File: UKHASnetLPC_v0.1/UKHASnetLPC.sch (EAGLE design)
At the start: 9 parts

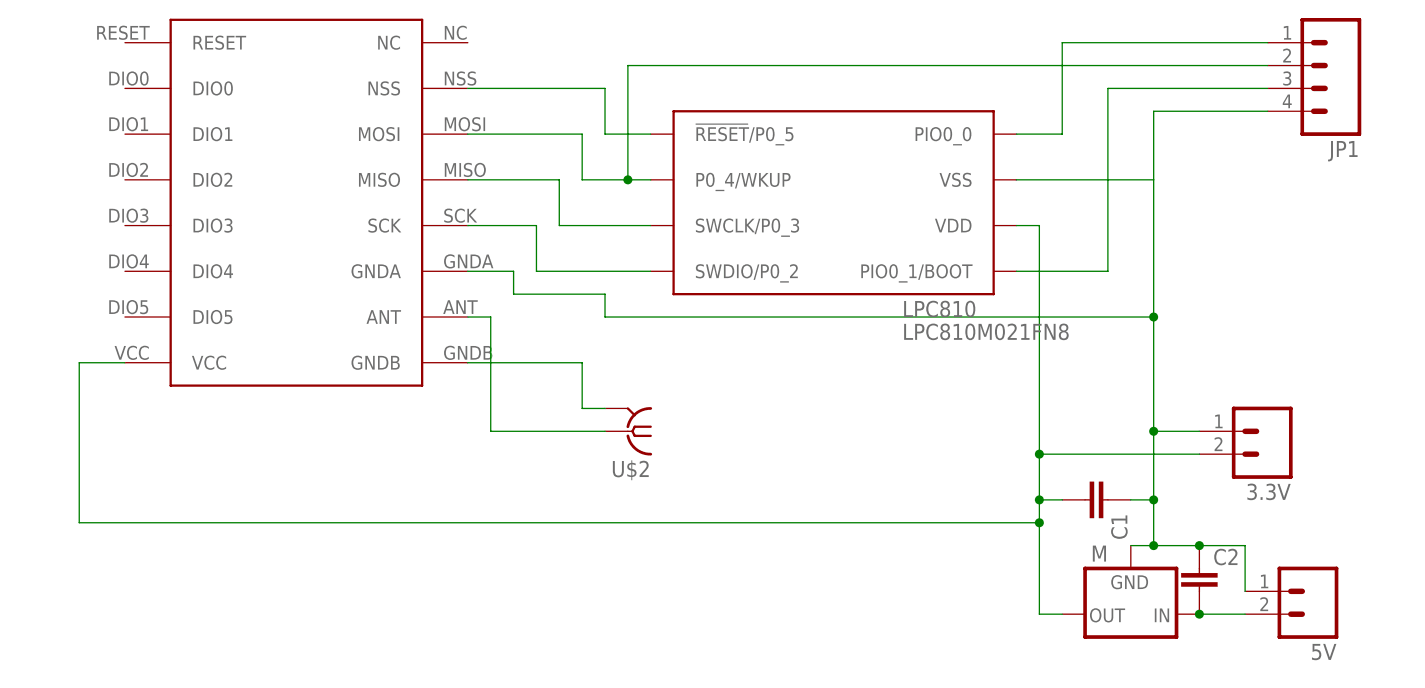
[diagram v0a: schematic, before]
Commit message: Redesigned board to avoid interference
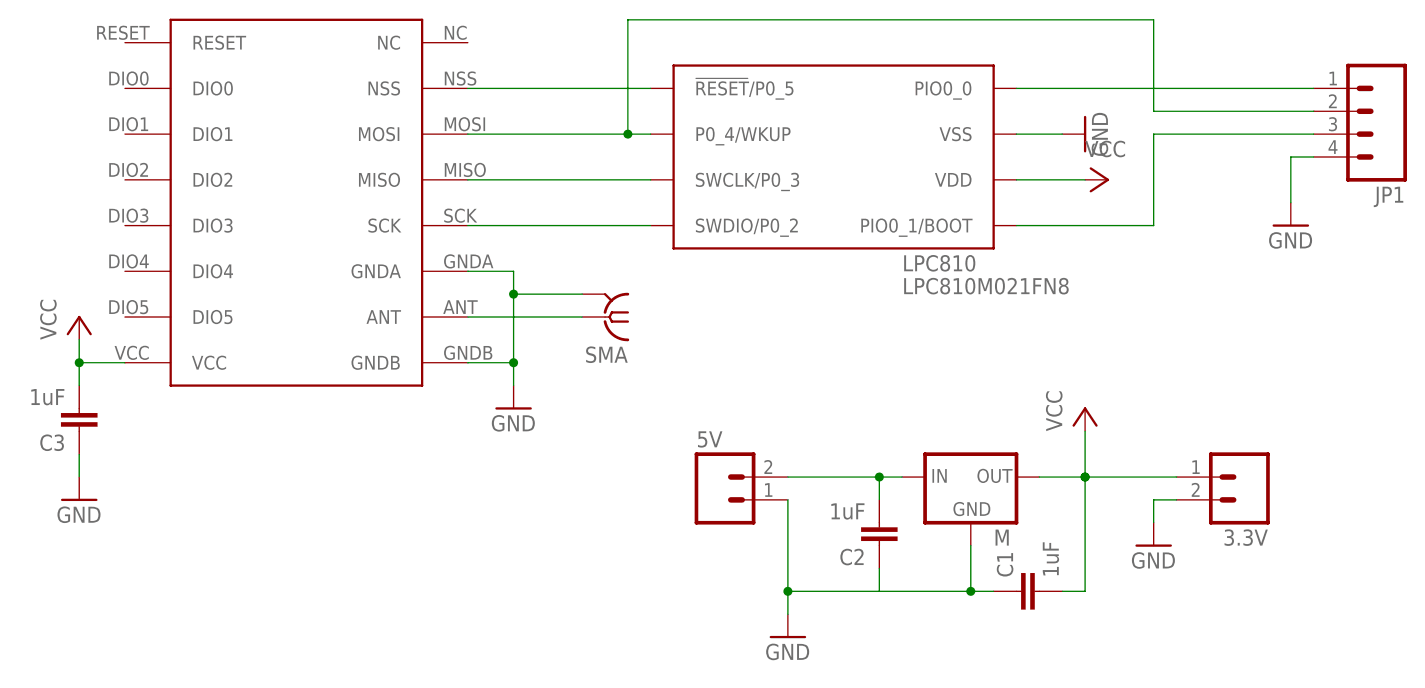
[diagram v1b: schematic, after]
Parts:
- removed U$2: BUS-SMA, Ava:BUS-SMA
- added C3: 1uF, SparkFun-Capacitors:CAPPTH
- added SMA: BUS-SMA, Ava:BUS-SMA
- C1, C2: value (none) -> 1uF
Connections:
- removed net N$12: 3.3V.2, C1.2, LPC810.VDD, M.OUT, RFM69.VCC
- removed net N$5: 3.3V.1, 5V.1, C1.1, C2.1, JP1.4, LPC810.VSS, M.GND, RFM69.GNDA
- new net VCC: 3.3V.1, C1.2, C3.2, LPC810.VDD, M.OUT, RFM69.VCC
- net GND: now also 3.3V.2, 5V.1, C1.1, C2.1, C3.1, JP1.4, LPC810.VSS, M.GND, RFM69.GNDA, SMA.GND; no longer U$2.GND
- net N$10: now also SMA.1; no longer U$2.1
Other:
- moved on the sheet: 3.3V, 5V, C1, C2, JP1, LPC810, M
